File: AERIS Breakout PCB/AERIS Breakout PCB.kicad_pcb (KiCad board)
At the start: 2 copper layers, 57 x 22 mm, 10 parts, among them J1 Conn_01x05_Socket, J2 Conn_01x02_Socket, J3 Conn_01x05_Socket, Q1 2N3904, U1 ESP32C3

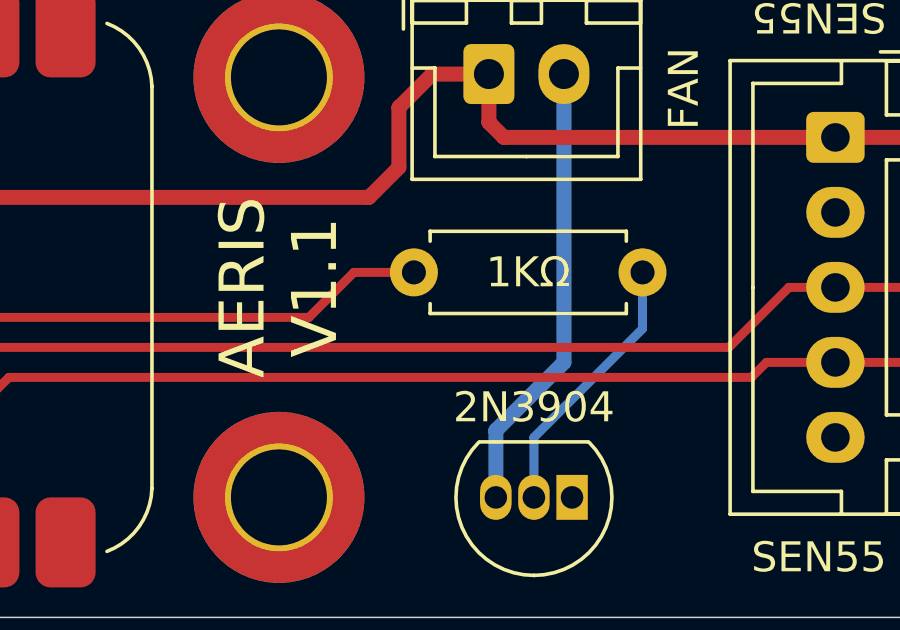
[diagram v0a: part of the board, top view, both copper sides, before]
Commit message: Update Breakout PCB To V1.2
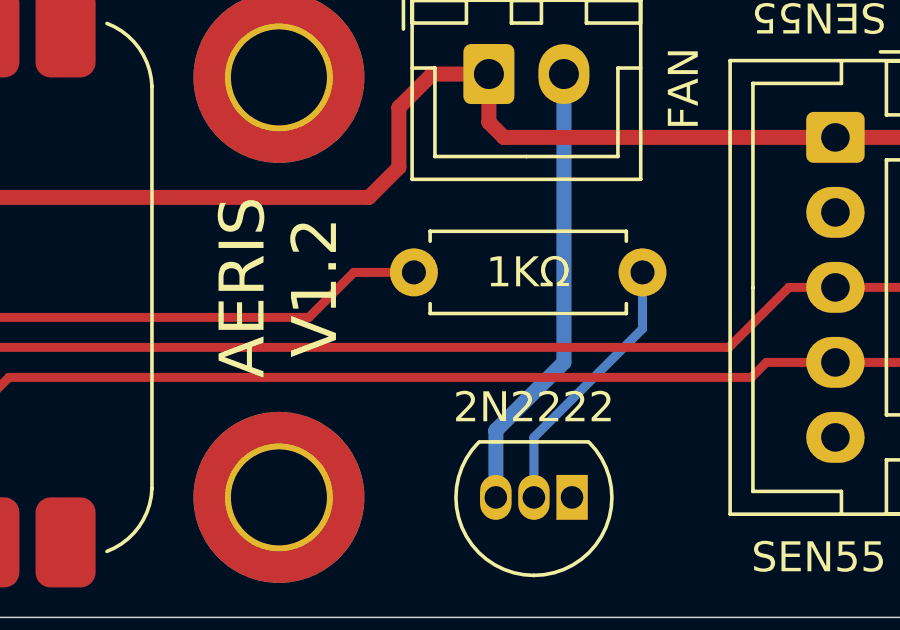
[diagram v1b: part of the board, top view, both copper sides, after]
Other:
- board text added: "+5V"
- board text added: "2N2222"
- board text added: "AERIS V1.2"
- board text removed: "2N3904"
- board text removed: "5V0"
- board text removed: "AERIS V1.1"
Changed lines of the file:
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@@
 			(plot_on_all_layers_selection 0x00000000_00000000_00000000_00000000)
 			(disableapertmacros no)
-			(usegerberextensions no)
+			(usegerberextensions yes)
 			(usegerberattributes yes)
 			(usegerberadvancedattributes yes)
@@
 		(net 3)
 	)
+	(gr_rect
+		(start 152.5 91.5)
+		(end 158 98)
+		(stroke
+			(width 0.1)
+			(type dash)
+		)
+		(fill no)
+		(layer "B.SilkS")
+	)
+	(gr_rect
+		(start 168.5 93.5)
+		(end 175 106.5)
+		(stroke
+			(width 0.1)
+			(type dash)
+		)
+		(fill no)
+		(layer "B.SilkS")
+	)
+	(gr_rect
+		(start 160.5 93.5)
+		(end 167 106.5)
+		(stroke
+			(width 0.1)
+			(type dash)
+		)
+		(fill no)
+		(layer "B.SilkS")
+	)
 	(gr_arc
 		(start 178 109)
@@
 		(layer "Edge.Cuts")
 	)
-	(gr_text "2N3904"
+	(gr_text "2N2222"
 		(at 155.5 104 0)
 		(layer "F.SilkS")
@@
 		)
 	)
-	(gr_text "AERIS\nV1.1"
+	(gr_text "AERIS\nV1.2"
 		(at 147 100 90)
 		(layer "F.SilkS")
@@
 	)
 	(gr_text "DISPLAY"
-		(at 173 108.913923 -180)
+		(at 171.75 108.913923 -180)
 		(layer "B.SilkS")
 		(effects
@@
 		)
 	)
-	(gr_text "5V0"
+	(gr_text "+5V"
 		(at 170.5 95 0)
 		(layer "B.SilkS")
@@
 	)
 	(gr_text "SEN55"
-		(at 164.999517 108.909187 -180)
+		(at 163.75 108.909187 -180)
 		(layer "B.SilkS")
 		(effects
@@
 		)
 	)
-	(gr_text "5V0"
+	(gr_text "+5V"
 		(at 154 96 90)
 		(layer "B.SilkS")
@@
 		)
 	)
-	(gr_text "5V0"
+	(gr_text "+5V"
 		(at 162.5 95 0)
 		(layer "B.SilkS")
@@
 	)
 	(gr_text "SEN55"
-		(at 165 91.087494 0)
+		(at 163.75 91.087494 0)
 		(layer "B.SilkS")
 		(effects
@@
 	)
 	(gr_text "DISPLAY"
-		(at 172.999445 91.088491 0)
+		(at 171.75 91.088491 0)
 		(layer "B.SilkS")
 		(effects
